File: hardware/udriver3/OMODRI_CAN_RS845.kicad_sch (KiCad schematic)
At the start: 12 parts, among them J13 conn_01x02_MountingPins, J16 Conn_01x02, U17 TCAN3413, U18 THVD24x0, U20 TS3USB221E

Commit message: Add snubbers on motors phases & resistors on high side gates. Update BOM list.
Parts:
- C101, C102, C105: DigiKey 490-14571-1-ND -> 490-12686-1-ND; Farnell 3790414 -> 2990693; LCSC C2649540 -> C76939; Mouser 81-GRM033R61E104KE4J -> 81-GRM033R61E104KE4D; Part No GRM033R61E104KE14J -> GRM033R61E104KE14D; RS 185-2066 -> (none)
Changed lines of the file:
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@@
 			)
 		)
-		(property "DigiKey" "490-14571-1-ND"
-			(at 88.9 144.78 0)
-			(effects
-				(font
-					(size 1.27 1.27)
-				)
-				(hide yes)
-			)
-		)
-		(property "Farnell" "3790414"
-			(at 88.9 144.78 0)
-			(effects
-				(font
-					(size 1.27 1.27)
-				)
-				(hide yes)
-			)
-		)
-		(property "Mouser" "81-GRM033R61E104KE4J"
-			(at 88.9 144.78 0)
-			(effects
-				(font
-					(size 1.27 1.27)
-				)
-				(hide yes)
-			)
-		)
-		(property "Part No" "GRM033R61E104KE14J"
-			(at 88.9 144.78 0)
-			(effects
-				(font
-					(size 1.27 1.27)
-				)
-				(hide yes)
-			)
-		)
-		(property "RS" "185-2066"
+		(property "DigiKey" "490-12686-1-ND"
+			(at 88.9 144.78 0)
+			(effects
+				(font
+					(size 1.27 1.27)
+				)
+				(hide yes)
+			)
+		)
+		(property "Farnell" "2990693"
+			(at 88.9 144.78 0)
+			(effects
+				(font
+					(size 1.27 1.27)
+				)
+				(hide yes)
+			)
+		)
+		(property "Mouser" "81-GRM033R61E104KE4D"
+			(at 88.9 144.78 0)
+			(effects
+				(font
+					(size 1.27 1.27)
+				)
+				(hide yes)
+			)
+		)
+		(property "Part No" "GRM033R61E104KE14D"
+			(at 88.9 144.78 0)
+			(effects
+				(font
+					(size 1.27 1.27)
+				)
+				(hide yes)
+			)
+		)
+		(property "RS" ""
 			(at 88.9 144.78 0)
 			(effects
@@
 			)
 		)
-		(property "LCSC" "C2649540"
+		(property "LCSC" "C76939"
 			(at 88.9 144.78 0)
 			(effects
@@
 			)
 		)
-		(property "DigiKey" "490-14571-1-ND"
-			(at 105.41 49.53 0)
-			(effects
-				(font
-					(size 1.27 1.27)
-				)
-				(hide yes)
-			)
-		)
-		(property "Farnell" "3790414"
-			(at 105.41 49.53 0)
-			(effects
-				(font
-					(size 1.27 1.27)
-				)
-				(hide yes)
-			)
-		)
-		(property "Mouser" "81-GRM033R61E104KE4J"
-			(at 105.41 49.53 0)
-			(effects
-				(font
-					(size 1.27 1.27)
-				)
-				(hide yes)
-			)
-		)
-		(property "Part No" "GRM033R61E104KE14J"
-			(at 105.41 49.53 0)
-			(effects
-				(font
-					(size 1.27 1.27)
-				)
-				(hide yes)
-			)
-		)
-		(property "RS" "185-2066"
+		(property "DigiKey" "490-12686-1-ND"
+			(at 105.41 49.53 0)
+			(effects
+				(font
+					(size 1.27 1.27)
+				)
+				(hide yes)
+			)
+		)
+		(property "Farnell" "2990693"
+			(at 105.41 49.53 0)
+			(effects
+				(font
+					(size 1.27 1.27)
+				)
+				(hide yes)
+			)
+		)
+		(property "Mouser" "81-GRM033R61E104KE4D"
+			(at 105.41 49.53 0)
+			(effects
+				(font
+					(size 1.27 1.27)
+				)
+				(hide yes)
+			)
+		)
+		(property "Part No" "GRM033R61E104KE14D"
+			(at 105.41 49.53 0)
+			(effects
+				(font
+					(size 1.27 1.27)
+				)
+				(hide yes)
+			)
+		)
+		(property "RS" ""
 			(at 105.41 49.53 0)
 			(effects
@@
 			)
 		)
-		(property "LCSC" "C2649540"
+		(property "LCSC" "C76939"
 			(at 105.41 49.53 0)
 			(effects
@@
 			)
 		)
-		(property "DigiKey" "490-14571-1-ND"
-			(at 187.96 111.76 0)
-			(effects
-				(font
-					(size 1.27 1.27)
-				)
-				(hide yes)
-			)
-		)
-		(property "Farnell" "3790414"
-			(at 187.96 111.76 0)
-			(effects
-				(font
-					(size 1.27 1.27)
-				)
-				(hide yes)
-			)
-		)
-		(property "Mouser" "81-GRM033R61E104KE4J"
-			(at 187.96 111.76 0)
-			(effects
-				(font
-					(size 1.27 1.27)
-				)
-				(hide yes)
-			)
-		)
-		(property "Part No" "GRM033R61E104KE14J"
-			(at 187.96 111.76 0)
-			(effects
-				(font
-					(size 1.27 1.27)
-				)
-				(hide yes)
-			)
-		)
-		(property "RS" "185-2066"
+		(property "DigiKey" "490-12686-1-ND"
+			(at 187.96 111.76 0)
+			(effects
+				(font
+					(size 1.27 1.27)
+				)
+				(hide yes)
+			)
+		)
+		(property "Farnell" "2990693"
+			(at 187.96 111.76 0)
+			(effects
+				(font
+					(size 1.27 1.27)
+				)
+				(hide yes)
+			)
+		)
+		(property "Mouser" "81-GRM033R61E104KE4D"
+			(at 187.96 111.76 0)
+			(effects
+				(font
+					(size 1.27 1.27)
+				)
+				(hide yes)
+			)
+		)
+		(property "Part No" "GRM033R61E104KE14D"
+			(at 187.96 111.76 0)
+			(effects
+				(font
+					(size 1.27 1.27)
+				)
+				(hide yes)
+			)
+		)
+		(property "RS" ""
 			(at 187.96 111.76 0)
 			(effects
@@
 			)
 		)
-		(property "LCSC" "C2649540"
-			(at 187.96 111.76 0)
-			(effects
+		(property "LCSC" "C76939"
+			(at 187.96 111.76 0)
+			(effects

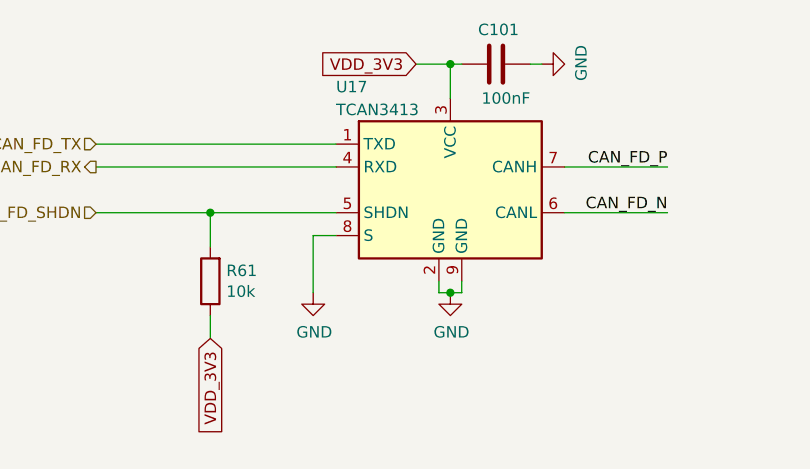
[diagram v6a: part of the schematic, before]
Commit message: Update of uOmodri_V3 replacing TCAN3413 by TCAN330G and adding sync on IMU.
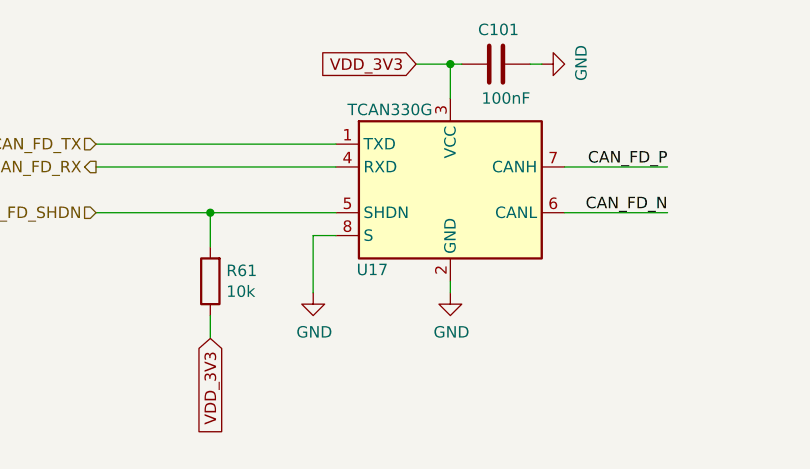
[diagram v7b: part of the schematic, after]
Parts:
- removed U17: TCAN3413, udriver3:VSON-8-1EP_3.0x3.0mm_P0.65mm_EP1.65x2.4mm, symbol omodri_lib:TCAN3413
- added U17: TCAN330G, Package_TO_SOT_SMD:SOT-23-8, symbol Interface_CAN_LIN:TCAN330G
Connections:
- net CAN_FD_N: now also U17.6 (CANL)
- net CAN_FD_P: now also U17.7 (CANH)
- net CAN_FD_RX: now also U17.4 (RXD)
- net CAN_FD_SHDN: now also U17.5 (SHDN)
- net CAN_FD_TX: now also U17.1 (TXD)
- net GND: now also U17.2 (GND), U17.8 (S)
- net VDD_3V3: now also U17.3 (VCC)
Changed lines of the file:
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@@
-	)
-	(junction
-		(at 100.33 74.93)
-		(diameter 0)
-		(color 0 0 0 0)
 	)
 	(junction
@@
 	(wire
 		(pts
-			(xy 101.6 73.66) (xy 101.6 74.93)
-		)
-		(stroke
-			(width 0)
-			(type default)
-		)
-	)
-	(wire
-		(pts
 			(xy 222.25 82.55) (xy 234.95 82.55)
 		)
@@
 	(wire
 		(pts
+			(xy 100.33 73.66) (xy 100.33 74.93)
+		)
+		(stroke
+			(width 0)
+			(type default)
+		)
+	)
+	(wire
+		(pts
 			(xy 88.9 138.43) (xy 88.9 140.97)
 		)
@@
 	(wire
 		(pts
-			(xy 99.06 74.93) (xy 100.33 74.93)
-		)
-		(stroke
-			(width 0)
-			(type default)
-		)
-	)
-	(wire
-		(pts
 			(xy 179.07 97.79) (xy 204.47 97.79)
 		)
@@
 	(wire
 		(pts
-			(xy 101.6 74.93) (xy 100.33 74.93)
-		)
-		(stroke
-			(width 0)
-			(type default)
-		)
-	)
-	(wire
-		(pts
 			(xy 73.66 77.47) (xy 73.66 80.01)
 		)
@@
 		(pts
 			(xy 85.09 68.58) (xy 85.09 74.93)
-		)
-		(stroke
-			(width 0)
-			(type default)
-		)
-	)
-	(wire
-		(pts
-			(xy 99.06 73.66) (xy 99.06 74.93)
 		)
 		(stroke
@@
 	)
 	(symbol
+		(lib_id "Interface_CAN_LIN:TCAN330G")
+		(at 100.33 63.5 0)
+		(unit 1)
+		(exclude_from_sim no)
+		(in_bom yes)
+		(on_board yes)
+		(dnp no)
+		(property "Reference" "U17"
+			(at 89.916 72.39 0)
+			(effects
+				(font
+					(size 1.27 1.27)
+				)
+				(justify left)
+			)
+		)
+		(property "Value" "TCAN330G"
+			(at 88.9 54.61 0)
+			(effects
+				(font
+					(size 1.27 1.27)
+				)
+				(justify left)
+			)
+		)
+		(property "Footprint" "Package_TO_SOT_SMD:SOT-23-8"
+			(at 100.33 76.2 0)
+			(effects
+				(font
+					(size 1.27 1.27)
+					(italic yes)
+				)
+				(hide yes)
+			)
+		)
+		(property "Datasheet" "http://www.ti.com/lit/ds/symlink/tcan337.pdf"
+			(at 100.33 63.5 0)
+			(effects
+				(font
+					(size 1.27 1.27)
+				)
+				(hide yes)
+			)
+		)
+		(property "Description" "High-Speed CAN Transceiver with CAN FD, 5Mbps, 3.3V supply, silent mode, shutdown mode, SOT-23-8/SOIC-8"
+			(at 100.33 63.5 0)
+			(effects
+				(font
+					(size 1.27 1.27)
+				)
+				(hide yes)
+			)
+		)
+		(pin "2"
+		)
+		(pin "5"
+		)
+		(pin "3"
+		)
+		(pin "1"
+		)
+		(pin "8"
+		)
+		(pin "7"
+		)
+		(pin "6"
+		)
+		(pin "4"
+		)
+		(instances
+			(project "omodri_laas"
+				(path "/de5b13f0-933a-4c4d-9979-13dc57b13241/f886a7a6-33d7-48db-abbb-6951d00de62d"
+					(reference "U17")
+					(unit 1)
+				)
+			)
+		)
+	)
+	(symbol
 		(lib_id "power:GND")
 		(at 111.76 149.86 0)
@@
 					(unit 1)
 				)
-			)
-		)
-	)
-	(symbol
-		(lib_id "omodri_lib:TCAN3413")
-		(at 100.33 63.5 0)
-		(unit 1)
-		(exclude_from_sim no)
-		(in_bom yes)
-		(on_board yes)
-		(dnp no)
-		(property "Reference" "U17"
-			(at 87.63 52.07 0)
-			(effects
-				(font
-					(size 1.27 1.27)
-				)
-				(justify left)
-			)
-		)
-		(property "Value" "TCAN3413"
-			(at 87.63 54.61 0)
-			(effects
-				(font
-					(size 1.27 1.27)
-				)
-				(justify left)
-			)
-		)
-		(property "Footprint" "udriver3:VSON-8-1EP_3.0x3.0mm_P0.65mm_EP1.65x2.4mm"
-			(at 100.33 63.5 0)
-			(effects
-				(font
-					(size 1.27 1.27)
-				)
-				(hide yes)
-			)
-		)
-		(property "Datasheet" "https://www.ti.com/lit/ds/symlink/tcan3413.pdf"
-			(at 100.33 82.55 0)
-			(effects
-				(font
-					(size 1.27 1.27)
-				)
-				(hide yes)
-			)
-		)
-		(property "Description" "3.3-V CAN FD transceiver with flexible IO and standby mode"
-			(at 100.33 63.5 0)
-			(effects
-				(font
-					(size 1.27 1.27)
-				)
-				(hide yes)
-			)
-		)
-		(property "Mouser" " 595-PTCAN3413DRBR"
-			(at 100.33 63.5 0)
-			(effects
-				(font
-					(size 1.27 1.27)
-				)
-				(hide yes)
-			)
-		)
-		(property "Part No" "PTCAN3413DRBR"
-			(at 100.33 63.5 0)
-			(effects
-				(font
-					(size 1.27 1.27)
-				)
-				(hide yes)
-			)
-		)
-		(property "LCSC" ""
-			(at 100.33 63.5 0)
-			(effects
-				(font
-					(size 1.27 1.27)
-				)
-				(hide yes)
-			)
-		)
-		(pin "3"
-		)
-		(pin "4"
-		)
-		(pin "7"
-		)
-		(pin "8"
-		)
-		(pin "6"
-		)
-		(pin "5"
-		)
-		(pin "2"
-		)
-		(pin "1"
-		)
-		(pin "9"
-		)
-		(instances
-			(project "omodri_laas"
-				(path "/de5b13f0-933a-4c4d-9979-13dc57b13241/f886a7a6-33d7-48db-abbb-6951d00de62d"
-					(reference "U17")
-					(unit 1)
-				)

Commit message: Update BOM list including TCAN refs. Update Gerber + pos + drills files.
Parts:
- U17: DigiKey (none) -> 296-TCAN330GDCNRCT-ND; LCSC (none) -> C191006; Mouser (none) -> 595-TCAN330GDCNR; Part No (none) -> TCAN330GDCNR
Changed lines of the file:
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@@
+			)
+		)
+		(property "DigiKey" "296-TCAN330GDCNRCT-ND"
+			(at 100.33 63.5 0)
+			(effects
+				(font
+					(size 1.27 1.27)
+				)
+				(hide yes)
+			)
+		)
+		(property "Part No" "TCAN330GDCNR"
+			(at 100.33 63.5 0)
+			(effects
+				(font
+					(size 1.27 1.27)
+				)
+				(hide yes)
+			)
+		)
+		(property "Mouser" "  595-TCAN330GDCNR"
+			(at 100.33 63.5 0)
+			(effects
+				(font
+					(size 1.27 1.27)
+				)
+				(hide yes)
+			)
+		)
+		(property "LCSC" "C191006"
+			(at 100.33 63.5 0)
+			(effects
+				(font
+					(size 1.27 1.27)
+				)
+				(hide yes)
 			)
 		)
